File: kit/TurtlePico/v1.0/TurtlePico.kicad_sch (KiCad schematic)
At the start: 40 parts, among them IC1 DRV8835DSSR, J1 USB-C, J10 LMotor, J11 Micro_SD, J12 FR_ESC, J13 FL_ESC, J14 RR_ESC, J15 RL_ESC, J2 AudioJack3, J3 LED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

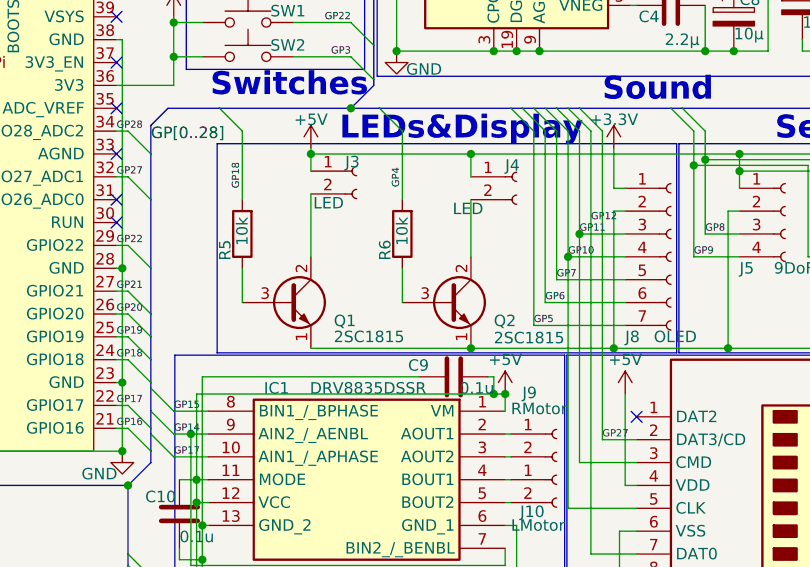
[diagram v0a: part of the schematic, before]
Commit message: change BJT and some design
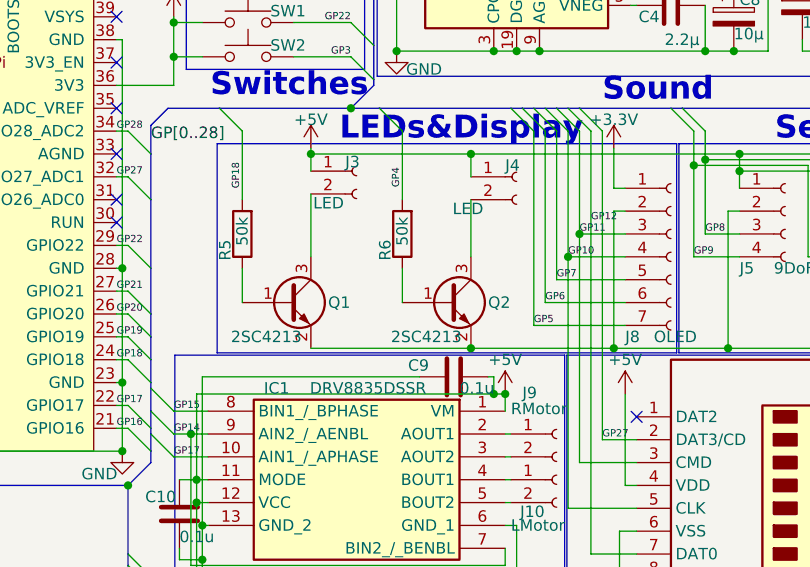
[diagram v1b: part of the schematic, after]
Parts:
- removed Q1, Q2: 2SC1815, Package_TO_SOT_SMD:SC-59, symbol Transistor_BJT:2SC1815
- added Q1, Q2: 2SC4213, Package_TO_SOT_SMD:SOT-323_SC-70, symbol Transistor_BJT:2SC4213
- R5, R6: value 10k -> 50k
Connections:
- net GND: now also Q1.2 (E), Q2.2 (E)
- net at J3.2 (Pin_2): now also Q1.3 (C)
- net at R5.1: now also Q1.1 (B)
- net at J4.2 (Pin_2): now also Q2.3 (C)
- net at R6.1: now also Q2.1 (B)

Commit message: update v1.1 fix usb
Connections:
- net at J1.B7 (DN2), U2.TP2 (USB_DM): now also J1.A7 (DN1); no longer J1.A6 (DP1)
- net at J1.B6 (DP2), U2.TP3 (USB_DP): now also J1.A6 (DP1); no longer J1.A7 (DN1)
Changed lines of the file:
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@@
   (junction (at 114.935 137.795) (diameter 0) (color 0 0 0 0)
   )
+  (junction (at 88.9 70.485) (diameter 0) (color 0 0 0 0)
+  )
   (junction (at 187.325 74.93) (diameter 0) (color 0 0 0 0)
   )
@@
   (junction (at 187.325 85.09) (diameter 0) (color 0 0 0 0)
   )
+  (junction (at 90.17 71.12) (diameter 0) (color 0 0 0 0)
+  )
   (junction (at 206.375 152.4) (diameter 0) (color 0 0 0 0)
   )
@@
   (junction (at 126.365 156.845) (diameter 0) (color 0 0 0 0)
   )
-  (junction (at 90.17 70.485) (diameter 0) (color 0 0 0 0)
-  )
   (junction (at 152.4 52.07) (diameter 0) (color 0 0 0 0)
   )
@@
   )
   (junction (at 114.3 132.715) (diameter 0) (color 0 0 0 0)
-  )
-  (junction (at 88.9 71.12) (diameter 0) (color 0 0 0 0)
   )
   (junction (at 185.42 118.11) (diameter 0) (color 0 0 0 0)
@@
     (stroke (width 0) (type default))
   )
-  (wire (pts (xy 86.36 70.485) (xy 90.17 70.485))
+  (wire (pts (xy 86.36 70.485) (xy 88.9 70.485))
     (stroke (width 0) (type default))
   )
@@
     (stroke (width 0) (type default))
   )
+  (wire (pts (xy 90.17 71.12) (xy 132.08 71.12))
+    (stroke (width 0) (type default))
+  )
   (wire (pts (xy 109.22 144.78) (xy 132.08 144.78))
     (stroke (width 0) (type default))
@@
     (stroke (width 0) (type default))
   )
+  (wire (pts (xy 88.9 55.88) (xy 88.9 70.485))
+    (stroke (width 0) (type default))
+  )
   (bus (pts (xy 66.04 129.54) (xy 66.04 130.81))
     (stroke (width 0) (type default))
@@
     (stroke (width 0) (type default))
   )
-  (wire (pts (xy 88.9 71.12) (xy 83.82 71.12))
+  (wire (pts (xy 83.82 71.12) (xy 90.17 71.12))
     (stroke (width 0) (type default))
   )
@@
     (stroke (width 0) (type default))
   )
+  (wire (pts (xy 88.9 70.485) (xy 132.715 70.485))
+    (stroke (width 0) (type default))
+  )
   (wire (pts (xy 91.44 55.88) (xy 88.9 55.88))
     (stroke (width 0) (type default))
@@
     (stroke (width 0) (type default))
   )
+  (wire (pts (xy 90.17 58.42) (xy 90.17 71.12))
+    (stroke (width 0) (type default))
+  )
   (bus (pts (xy 66.04 119.38) (xy 66.04 121.92))
     (stroke (width 0) (type default))
@@
     (stroke (width 0) (type default))
   )
-  (wire (pts (xy 132.08 71.12) (xy 88.9 71.12))
-    (stroke (width 0) (type default))
-  )
   (wire (pts (xy 154.305 93.98) (xy 154.305 110.49))
     (stroke (width 0) (type default))
@@
     (stroke (width 0) (type default))
   )
-  (wire (pts (xy 90.17 70.485) (xy 132.715 70.485))
-    (stroke (width 0) (type default))
-  )
   (wire (pts (xy 131.445 149.86) (xy 131.445 142.875))
     (stroke (width 0) (type default))
@@
     (stroke (width 0) (type default))
   )
-  (wire (pts (xy 88.9 55.88) (xy 88.9 71.12))
-    (stroke (width 0) (type default))
-  )
   (wire (pts (xy 183.515 102.87) (xy 183.515 97.155))
     (stroke (width 0) (type default))
@@
     (stroke (width 0) (type default))
   )
-  (wire (pts (xy 90.17 58.42) (xy 90.17 70.485))
-    (stroke (width 0) (type default))
-  )

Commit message: update v.1 change uart and ultrasonic pin
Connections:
- net GP0: now also J7.2 (Pin_2); no longer R7.2, R8.1
- net GP1: now also R7.2, R8.1; no longer J7.2 (Pin_2)
- no-connect marks 19 -> 18
